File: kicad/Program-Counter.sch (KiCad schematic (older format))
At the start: 6 parts, among them U131 74LS161, U132 74LS161, U133 74LS161, U134 74LS161, U135 74LS245, U136 74LS245

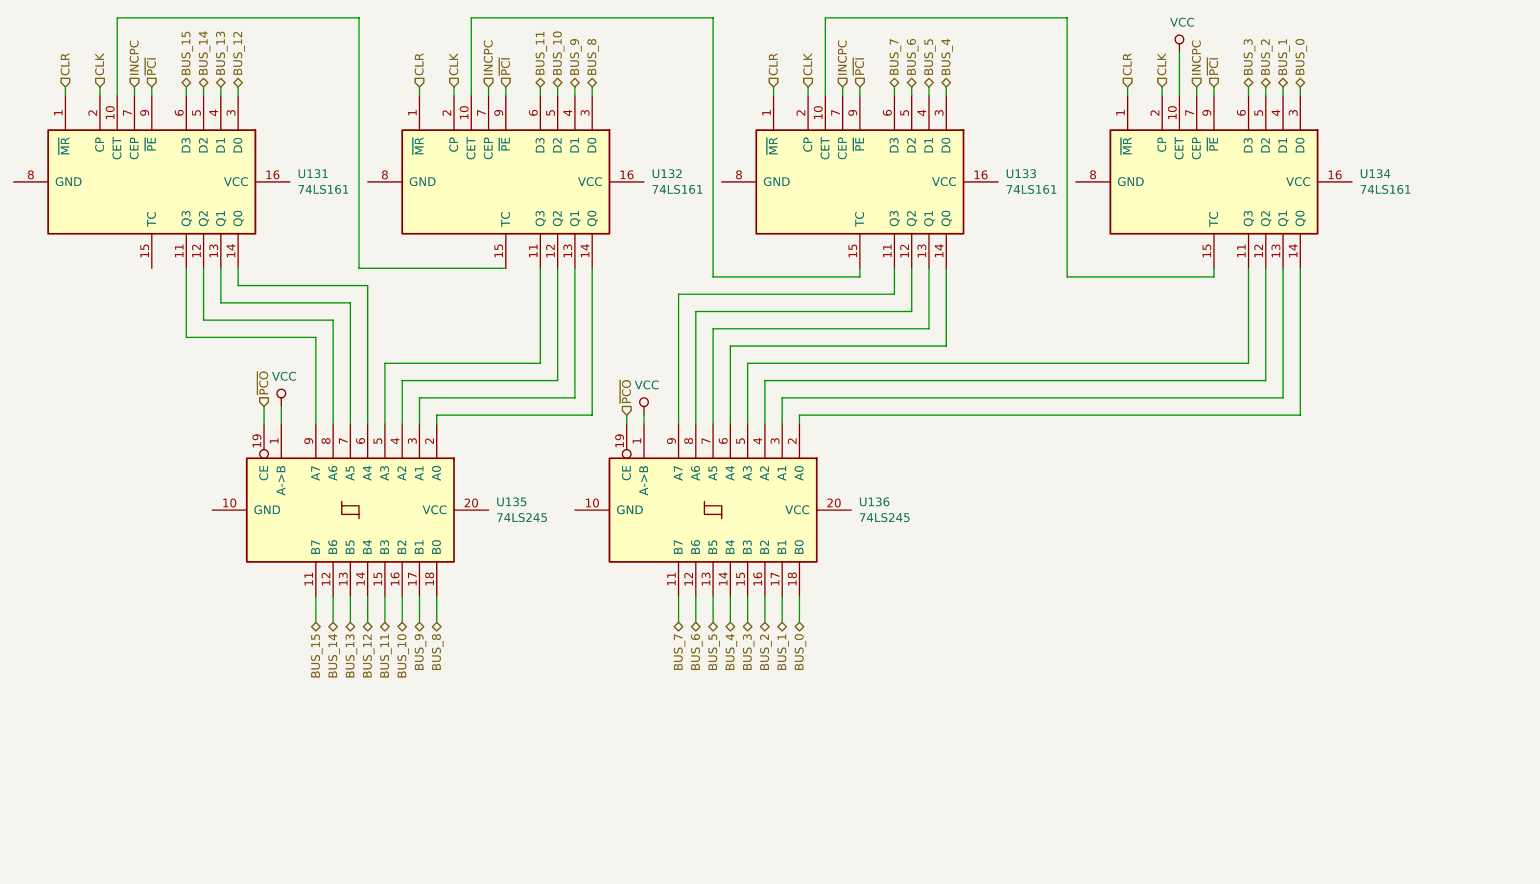
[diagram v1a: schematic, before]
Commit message: Reorganize part references
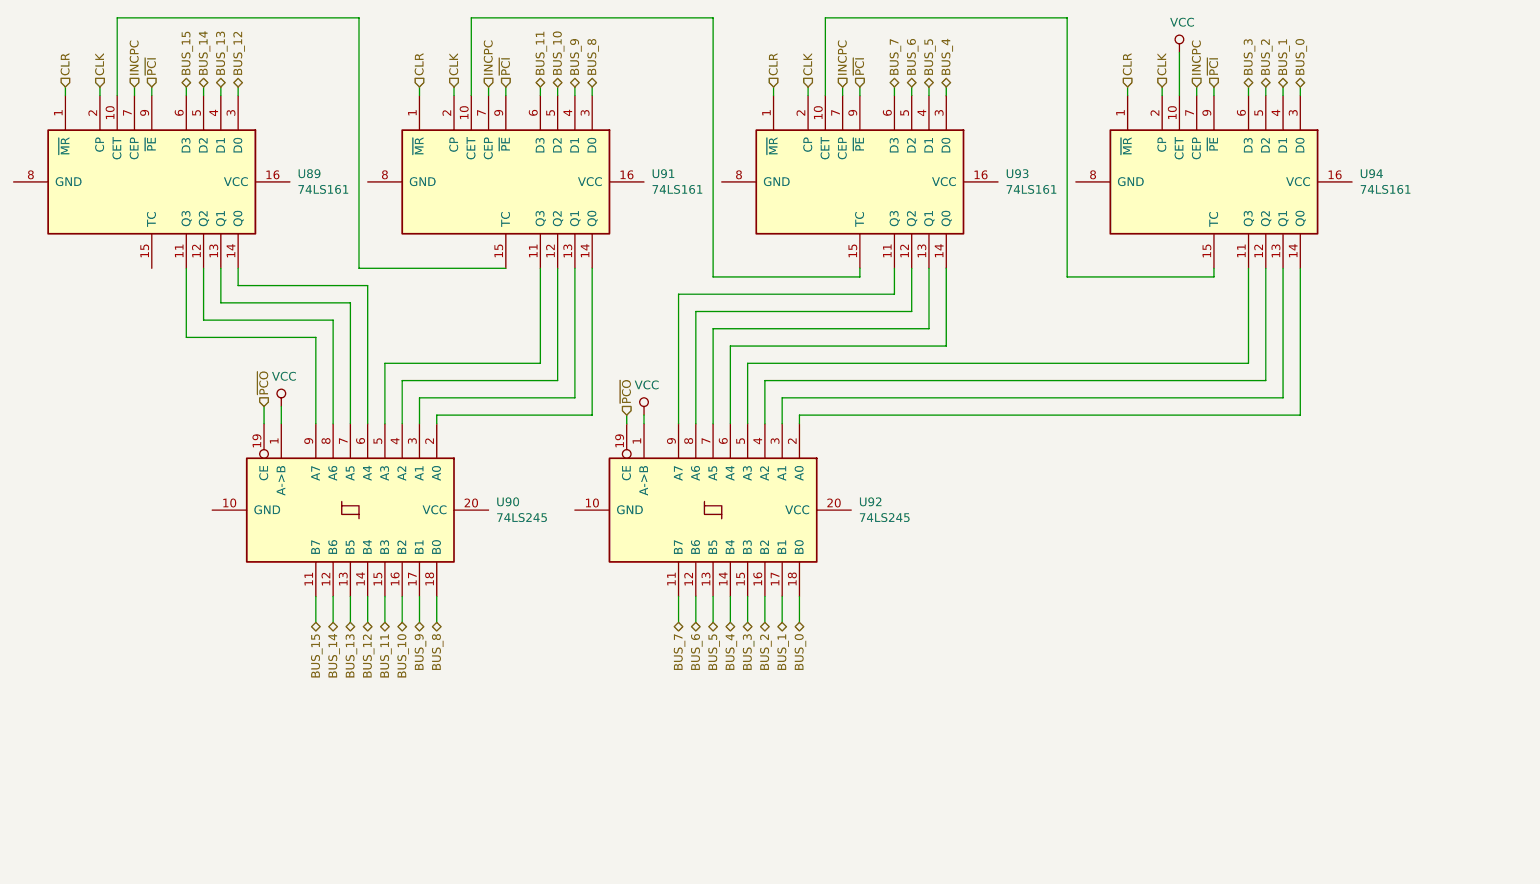
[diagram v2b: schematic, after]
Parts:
- renumbered U131 to U89, U135 to U90, U132 to U91, U136 to U92, U133 to U93, U134 to U94
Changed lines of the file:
@@
 ~PCI~
 $Comp
-L 74xx:74LS161 U131
+L 74xx:74LS161 U89
 U 1 1 605241F8
 P 1950 1950
-F 0 "U131" V 1904 2794 50  0000 L CNN
+F 0 "U89" V 1904 2794 50  0000 L CNN
 F 1 "74LS161" V 1995 2794 50  0000 L CNN
 F 2 "" H 1950 1950 50  0001 C CNN
@@
 $EndComp
 $Comp
-L 74xx:74LS161 U132
+L 74xx:74LS161 U91
 U 1 1 60528F0E
 P 4000 1950
-F 0 "U132" V 3954 2794 50  0000 L CNN
+F 0 "U91" V 3954 2794 50  0000 L CNN
 F 1 "74LS161" V 4045 2794 50  0000 L CNN
 F 2 "" H 4000 1950 50  0001 C CNN
@@
 $EndComp
 $Comp
-L 74xx:74LS161 U133
+L 74xx:74LS161 U93
 U 1 1 6052CF75
 P 6050 1950
-F 0 "U133" V 6004 2794 50  0000 L CNN
+F 0 "U93" V 6004 2794 50  0000 L CNN
 F 1 "74LS161" V 6095 2794 50  0000 L CNN
 F 2 "" H 6050 1950 50  0001 C CNN
@@
 $EndComp
 $Comp
-L 74xx:74LS161 U134
+L 74xx:74LS161 U94
 U 1 1 6052CF7B
 P 8100 1950
-F 0 "U134" V 8054 2794 50  0000 L CNN
+F 0 "U94" V 8054 2794 50  0000 L CNN
 F 1 "74LS161" V 8145 2794 50  0000 L CNN
 F 2 "" H 8100 1950 50  0001 C CNN
@@
 	1750 1000 1750 1450
 $Comp
-L 74xx:74LS245 U135
+L 74xx:74LS245 U90
 U 1 1 60546328
 P 3100 3850
-F 0 "U135" V 3054 4694 50  0000 L CNN
+F 0 "U90" V 3054 4694 50  0000 L CNN
 F 1 "74LS245" V 3145 4694 50  0000 L CNN
 F 2 "" H 3100 3850 50  0001 C CNN
@@
 $EndComp
 $Comp
-L 74xx:74LS245 U136
+L 74xx:74LS245 U92
 U 1 1 6054B8F9
 P 5200 3850
-F 0 "U136" V 5154 4694 50  0000 L CNN
+F 0 "U92" V 5154 4694 50  0000 L CNN
 F 1 "74LS245" V 5245 4694 50  0000 L CNN
 F 2 "" H 5200 3850 50  0001 C CNN

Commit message: Up to v1.0 and plot
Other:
- moved on the sheet: U89, U90, U91, U92, U93, U94
